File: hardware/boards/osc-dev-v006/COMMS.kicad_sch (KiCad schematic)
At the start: 10 parts, among them J10 PIN-1-3P, J11 JST-PH-V, J9 PIN-1-3P, U4 74LVC2G241

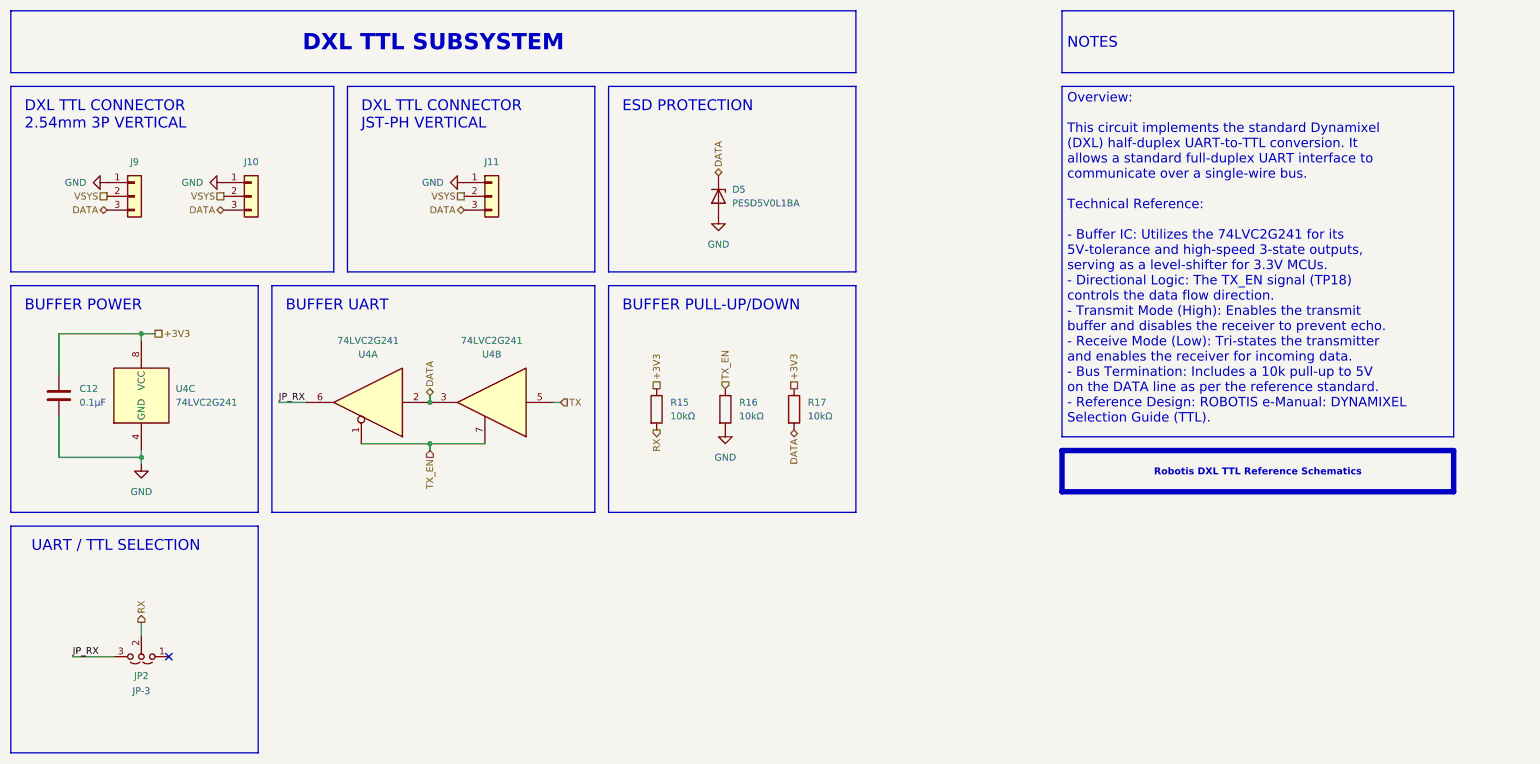
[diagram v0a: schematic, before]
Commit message: hw: osc-dev-v006 rev-2a - 6l precision respin, direct-wire bus, docs
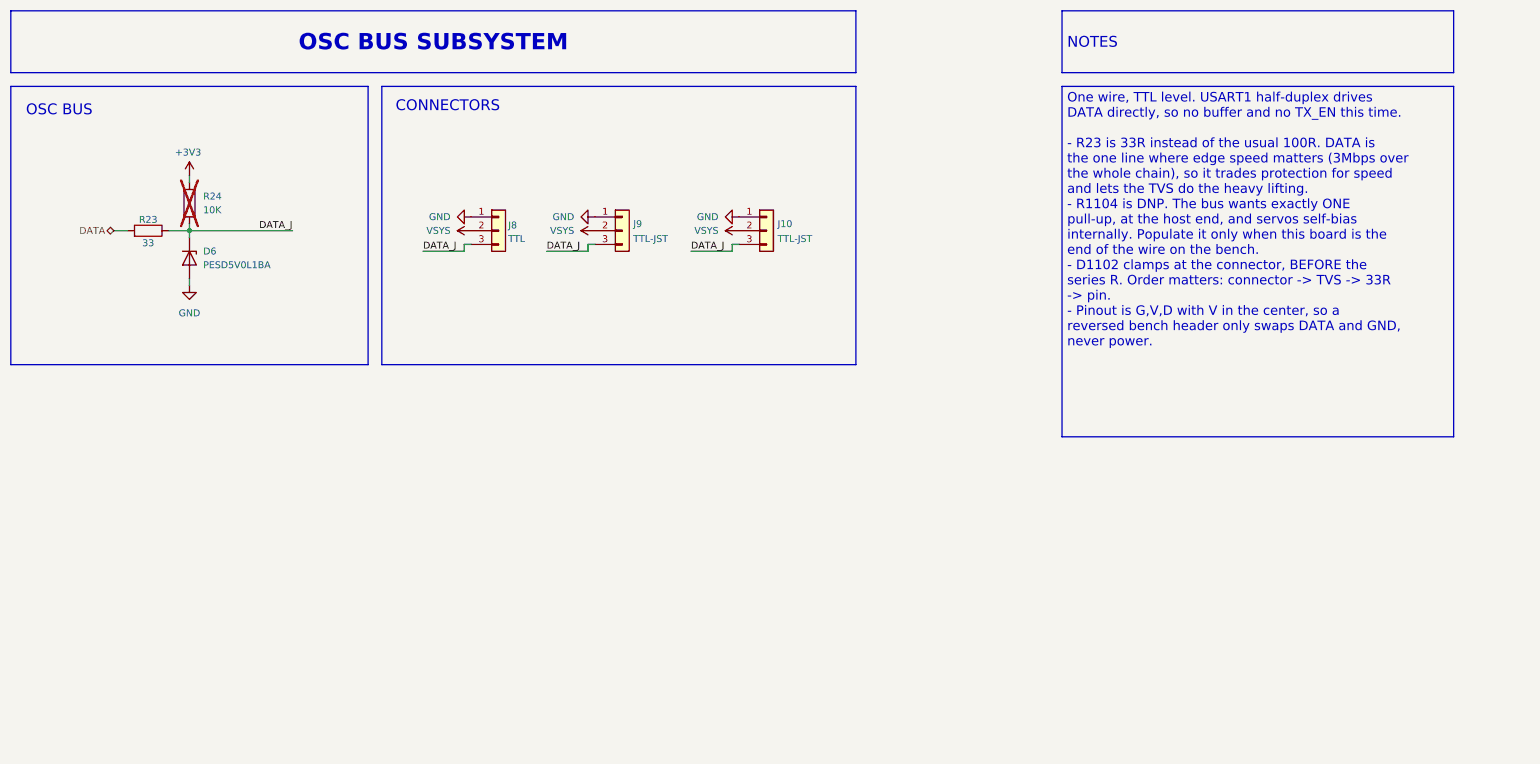
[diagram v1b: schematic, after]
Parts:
- removed C12: 0.1µF, Capacitor_SMD:C_0805_2012Metric_Pad1.18x1.45mm_HandSolder, symbol Device:C
- removed D5: PESD5V0L1BA, Diode_SMD:D_SOD-323_HandSoldering, symbol Diode:PESD5V0L1UL
- removed J11: JST-PH-V, shared:CONN-TH_B3B-PH-K-S, symbol Connector_Generic:Conn_01x03
- removed JP2: JP-3, Connector_PinHeader_2.54mm:PinHeader_1x03_P2.54mm_Vertical, symbol Jumper:Jumper_3_Open
- removed R15, R16, R17: 10kΩ, Resistor_SMD:R_0805_2012Metric_Pad1.20x1.40mm_HandSolder, symbol Device:R
- removed U4: 74LVC2G241, shared:VSSOP-8_L2.3-W2.0-P0.50-LS3.1-BR, symbol 74xGxx:74LVC2G241
- added D6: PESD5V0L1BA, Diode_SMD:D_SOD-323_HandSoldering, symbol Diode:PESD5V0L1UL
- added J9: TTL-JST, shared:CONN-TH_B3B-PH-K-S, symbol Connector_Generic:Conn_01x03
- added R23: 33, Resistor_SMD:R_0603_1608Metric_Pad0.98x0.95mm_HandSolder, symbol Device:R
- added R24: 10K, Resistor_SMD:R_0603_1608Metric_Pad0.98x0.95mm_HandSolder, symbol Device:R
- J10: value PIN-1-3P -> TTL-JST; footprint Connector_PinHeader_2.54mm:PinHeader_1x03_P2.54mm_Vertical -> shared:CONN-TH_B3B-PH-K-S; JLC Type (none) -> Extended; LCSC C49257 -> C131339; MFPN 2.54-1*3P -> B3B-PH-K-S(LF)(SN)
- J8: renamed from J9; value PIN-1-3P -> TTL
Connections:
- net +3V3: now also R24.1
- net DATA: now also R23.2; no longer J10.3 (Pin_3), J8.3 (Pin_3)
- net GND: now also D6.2 (A), J9.1 (Pin_1)
- net VSYS: now also J9.2 (Pin_2)
- new net DATA_J: D6.1 (K), J10.3 (Pin_3), J8.3 (Pin_3), J9.3 (Pin_3), R23.1, R24.2
- no-connect marks 1 -> 0
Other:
- note added: "CONNECTORS"
- note added: "OSC BUS"
- note removed: "BUFFER POWER"
- note removed: "BUFFER PULL-UP/DOWN"
- note removed: "BUFFER UART"
- note removed: "DXL TTL CONNECTOR 2.54mm 3P VERTICAL"
- note removed: "DXL TTL CONNECTOR JST-PH VERTICAL"
- note removed: "ESD PROTECTION"
- note removed: "UART / TTL SELECTION"
- title: (none) -> ${PROJECT} / ${BOARD}
- moved on the sheet: J8

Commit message: board: osc-dev-v006 rev 2a (#107)
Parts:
- Dx1: renamed from D6; JLC Type Extended -> (none); JLC_Basic no -> (none)
- J10, J9: JLC Type Extended -> (none)
- Rx1: renamed from R23; JLC_Basic yes -> (none); MFPN FRC0805F33R0TS -> RC0603FR-0733RL
- Rx2: renamed from R24; JLC_Basic yes -> (none); MFPN FRC0805F1002TS -> FRC0603F1002TS
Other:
- note added: "Bus connectors"
- note added: "One-wire bus"
- note removed: "CONNECTORS"
- note removed: "OSC BUS"
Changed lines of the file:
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@@
 		)
 	)
-	(text "CONNECTORS"
+	(text "Bus connectors"
 		(exclude_from_sim no)
 		(at 86.36 31.75 0)
@@
 		)
 	)
-	(text "OSC BUS"
+	(text "One-wire bus"
 		(exclude_from_sim no)
 		(at 18.034 32.512 0)
@@
 		)
 	)
-	(text_box "One wire, TTL level. USART1 half-duplex drives DATA directly, so no buffer and no TX_EN this time.\n\n- R23 is 33R instead of the usual 100R. DATA is the one line where edge speed matters (3Mbps over the whole chain), so it trades protection for speed and lets the TVS do the heavy lifting.\n- R1104 is DNP. The bus wants exactly ONE pull-up, at the host end, and servos self-bias internally. Populate it only when this board is the end of the wire on the bench.\n- D1102 clamps at the connector, BEFORE the series R. Order matters: connector -> TVS -> 33R -> pin.\n- Pinout is G,V,D with V in the center, so a reversed bench header only swaps DATA and GND, never power."
+	(text_box "One wire, TTL level. USART1 half-duplex drives DATA directly, so no buffer and no TX_EN this time. Telemetry rides this same wire as bounded CRC'd bursts, so there is no second UART on the board.\n\n- Rx1 is 33R instead of the usual 100R. DATA is the one line where edge speed matters (3Mbps over the whole chain), so it trades protection for speed and lets the TVS do the heavy lifting.\n- Rx2 is DNP. The bus wants exactly ONE pull-up, at the host end, and servos self-bias internally. Populate it only when this board is the end of the wire on the bench.\n- Dx1 clamps at the connector, BEFORE the series R. Order matters: connector -> TVS -> 33R -> pin.\n- Pinout is G,V,D with V in the center, so a reversed bench header only swaps DATA and GND, never power. V+ is VSYS straight through, unprotected."
 		(exclude_from_sim yes)
 		(at 209.55 29.21 0)
@@
 		)
 		(property "Description" "Generic connector, single row, 01x03, script generated (kicad-library-utils/schlib/autogen/connector/)"
-			(at 128.27 55.88 0)
-			(hide yes)
-			(show_name no)
-			(do_not_autoplace no)
-			(effects
-				(font
-					(size 1.27 1.27)
-				)
-			)
-		)
-		(property "JLC Type" "Extended"
 			(at 128.27 55.88 0)
 			(hide yes)
@@
 		(dnp yes)
 		(fields_autoplaced yes)
-		(property "Reference" "R24"
+		(property "Reference" "Rx2"
 			(at 50.8 49.5299 0)
 			(show_name no)
@@
 			)
 		)
-		(property "MFPN" "FRC0805F1002TS"
-			(at 50.8 49.5299 0)
-			(hide yes)
-			(show_name no)
-			(do_not_autoplace no)
-			(effects
-				(font
-					(size 1.27 1.27)
-				)
-			)
-		)
-		(property "JLC_Basic" "yes"
+		(property "MFPN" "FRC0603F1002TS"
 			(at 50.8 49.5299 0)
 			(hide yes)
@@
 			(project "osc-dev-v006"
 				(path "/6062e7d2-0c72-467e-b49c-6387ba053e09/d650f1be-e012-4c20-9ca8-eaa5ec4968ee"
-					(reference "R24")
+					(reference "Rx2")
 					(unit 1)
 				)
@@
 		(in_pos_files yes)
 		(dnp no)
-		(property "Reference" "R23"
+		(property "Reference" "Rx1"
 			(at 40.64 53.848 90)
 			(show_name no)
@@
 			)
 		)
-		(property "MFPN" "FRC0805F33R0TS"
-			(at 41.9101 53.34 0)
-			(hide yes)
-			(show_name no)
-			(do_not_autoplace no)
-			(effects
-				(font
-					(size 1.27 1.27)
-				)
-			)
-		)
-		(property "JLC_Basic" "yes"
+		(property "MFPN" "RC0603FR-0733RL"
 			(at 41.9101 53.34 0)
 			(hide yes)
@@
 			(project "osc-dev-v006"
 				(path "/6062e7d2-0c72-467e-b49c-6387ba053e09/d650f1be-e012-4c20-9ca8-eaa5ec4968ee"
-					(reference "R23")
+					(reference "Rx1")
 					(unit 1)
 				)
@@
 		(in_pos_files yes)
 		(dnp no)
-		(property "Reference" "D6"
+		(property "Reference" "Dx1"
 			(at 50.8 59.6899 90)
 			(show_name no)
@@
 		)
 		(property "MFPN" "PESD5V0L1BA"
-			(at 48.26 60.96 90)
-			(hide yes)
-			(show_name no)
-			(do_not_autoplace no)
-			(effects
-				(font
-					(size 1.27 1.27)
-				)
-			)
-		)
-		(property "JLC_Basic" "no"
-			(at 48.26 60.96 0)
-			(hide yes)
-			(show_name no)
-			(do_not_autoplace no)
-			(effects
-				(font
-					(size 1.27 1.27)
-				)
-			)
-		)
-		(property "JLC Type" "Extended"
 			(at 48.26 60.96 90)
 			(hide yes)
@@
 			(project "osc-dev-v006"
 				(path "/6062e7d2-0c72-467e-b49c-6387ba053e09/d650f1be-e012-4c20-9ca8-eaa5ec4968ee"
-					(reference "D6")
+					(reference "Dx1")
 					(unit 1)
 				)
@@
 			(at 154.94 55.88 0)
 			(hide yes)
-			(show_name no)
-			(do_not_autoplace no)
-			(effects
-				(font
-					(size 1.27 1.27)
-				)
-			)
-		)
-		(property "JLC Type" "Extended"
-			(at 154.94 55.88 0)
-			(hide yes)
